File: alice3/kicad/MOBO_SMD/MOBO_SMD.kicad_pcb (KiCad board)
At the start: 2 copper layers, 90.2 x 48.3 mm, 67 parts, among them CON1 MicroSD, J1 VGA, P1 CONN_01X05, P2 USB_OTG, P3 UART1, SW1 RESET, SW2 SOFT RESET, U1 Z80CPU-SMD, U2 Propeller_P8X32A-Q44, U3 24LC256, U4 Propeller_Plug, U5 STM32F415RG, U6 AS6C2008_TSOP, U8 LD29080DT33R, X1 MINI_DIN_6, Y1 5 MHz, Y2 16MHz

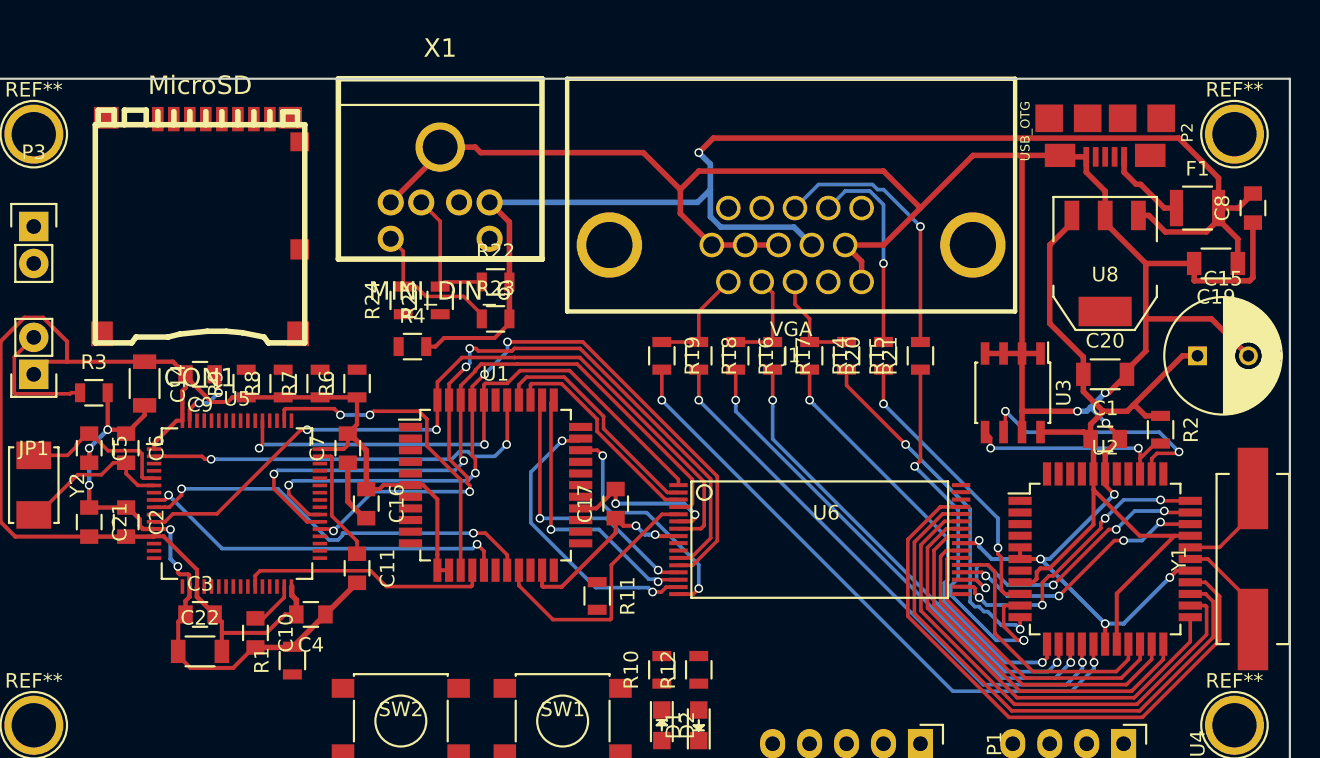
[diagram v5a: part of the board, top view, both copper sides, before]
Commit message: Switch to new MicroSD footprint and new Prop crystal.
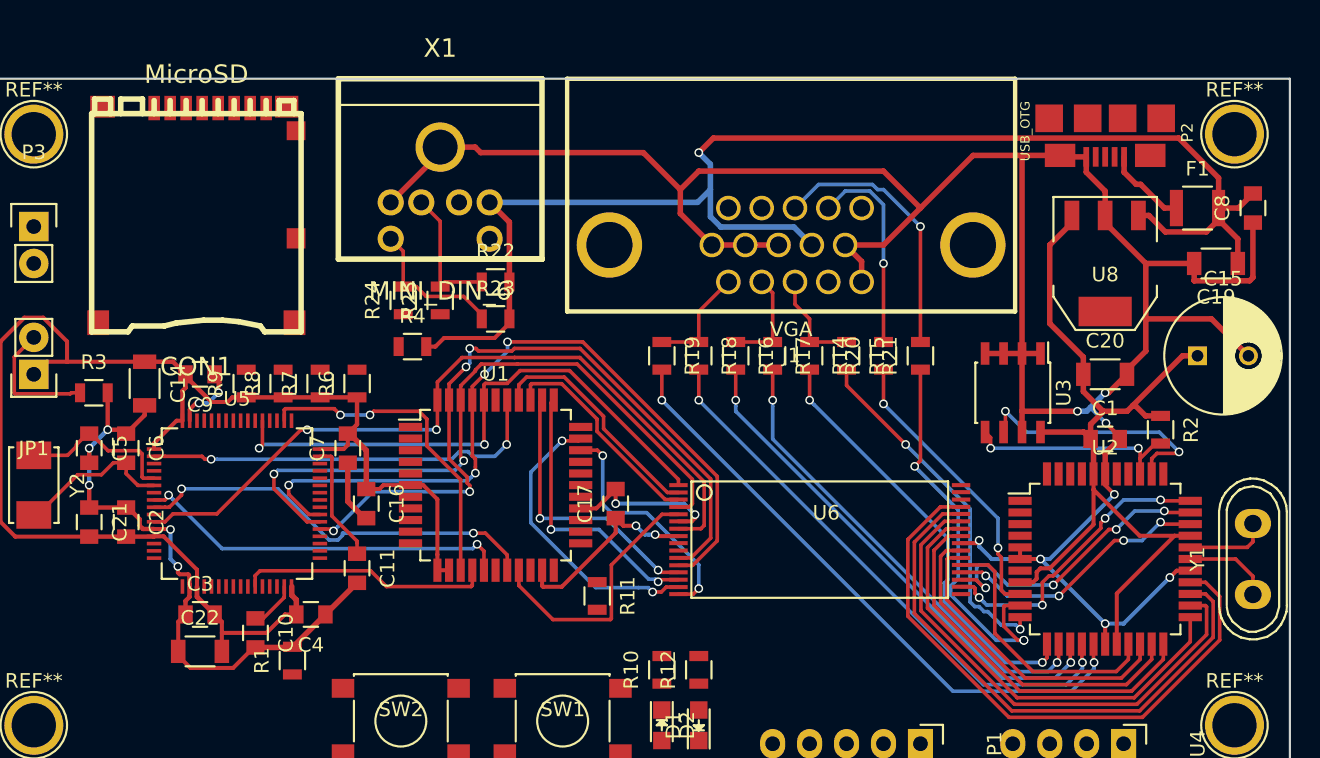
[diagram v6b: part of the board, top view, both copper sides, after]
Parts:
- Y1: footprint Crystals:Crystal_HC49-SD_SMD -> Crystals:Crystal_HC50-U_Vertical
- moved CON1 0.80 mm to (124.2, 83.1)
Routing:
- net Net-(U2-Pad28): track 7.34 -> 6.05 mm
- net Net-(U2-Pad29): track 7.01 -> 5.72 mm
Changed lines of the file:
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@@
   (general
     (links 246)
-    (no_connects 145)
-    (area 100.285476 67.307599 232.63921 175.29)
+    (no_connects 97)
+    (area 109.144999 73.584999 199.465001 121.995001)
     (thickness 1.6)
     (drawings 4)
@@
   )
   (module microsd:microsd_socket (layer F.Cu)
-    (at 124.46 83.82)
+    (at 124.206 83.058)
     (descr "MicroSD Card socket, Molex P/N 502774-0811")
     (fp_text reference CON1 (at 0 10.39876) (layer F.SilkS)
@@
       (net 100 "Net-(X1-Pad2)"))
   )
-  (module Crystals:Crystal_HC49-SD_SMD (layer F.Cu)
-    (at 196.85 106.68 90)
-    (descr "Crystal, Quarz, HC49-SD, SMD,")
-    (tags "Crystal, Quarz, HC49-SD, SMD,")
-    (attr smd)
-    (fp_text reference Y1 (at 0 -5.08 90) (layer F.SilkS)
-      (effects (font (size 1 1) (thickness 0.15)))
-    )
-    (fp_text value "5 MHz" (at 2.54 5.08 90) (layer F.Fab)
-      (effects (font (size 1 1) (thickness 0.15)))
-    )
-    (fp_circle (center 0 0) (end 0.8509 0) (layer F.Adhes) (width 0.381))
-    (fp_circle (center 0 0) (end 0.50038 0) (layer F.Adhes) (width 0.381))
-    (fp_circle (center 0 0) (end 0.14986 0.0508) (layer F.Adhes) (width 0.381))
-    (fp_line (start -5.84962 2.49936) (end 5.84962 2.49936) (layer F.SilkS) (width 0.15))
-    (fp_line (start 5.84962 -2.49936) (end -5.84962 -2.49936) (layer F.SilkS) (width 0.15))
-    (fp_line (start 5.84962 2.49936) (end 5.84962 1.651) (layer F.SilkS) (width 0.15))
-    (fp_line (start 5.84962 -2.49936) (end 5.84962 -1.651) (layer F.SilkS) (width 0.15))
-    (fp_line (start -5.84962 2.49936) (end -5.84962 1.651) (layer F.SilkS) (width 0.15))
-    (fp_line (start -5.84962 -2.49936) (end -5.84962 -1.651) (layer F.SilkS) (width 0.15))
-    (pad 1 smd rect (at -4.84886 0 90) (size 5.6007 2.10058) (layers F.Cu F.Paste F.Mask)
-      (net 93 "Net-(U2-Pad28)"))
-    (pad 2 smd rect (at 4.84886 0 90) (size 5.6007 2.10058) (layers F.Cu F.Paste F.Mask)
-      (net 94 "Net-(U2-Pad29)"))
-  )
   (module Crystals:ABM3 (layer F.Cu)
     (at 113.03 101.6 270)
@@
     (pad 1 thru_hole circle (at 0 0) (size 4.064 4.064) (drill 3.048) (layers *.Cu *.Mask F.SilkS))
   )
+  (module Crystals:Crystal_HC50-U_Vertical (layer F.Cu)
+    (at 196.85 106.68 90)
+    (descr "Crystal, Quarz, HC50/U, vertical, stehend,")
+    (tags "Crystal, Quarz, HC50/U, vertical, stehend,")
+    (fp_text reference Y1 (at 0 -3.81 90) (layer F.SilkS)
+      (effects (font (size 1 1) (thickness 0.15)))
+    )
+    (fp_text value "5 MHz" (at 0 3.81 90) (layer F.Fab)
+      (effects (font (size 1 1) (thickness 0.15)))
+    )
+    (fp_line (start 4.699 -1.00076) (end 4.89966 -0.59944) (layer F.SilkS) (width 0.15))
+    (fp_line (start 4.89966 -0.59944) (end 5.00126 0) (layer F.SilkS) (width 0.15))
+    (fp_line (start 5.00126 0) (end 4.89966 0.50038) (layer F.SilkS) (width 0.15))
+    (fp_line (start 4.89966 0.50038) (end 4.50088 1.19888) (layer F.SilkS) (width 0.15))
+    (fp_line (start 4.50088 1.19888) (end 3.8989 1.6002) (layer F.SilkS) (width 0.15))
+    (fp_line (start 3.8989 1.6002) (end 3.29946 1.80086) (layer F.SilkS) (width 0.15))
+    (fp_line (start 3.29946 1.80086) (end -3.29946 1.80086) (layer F.SilkS) (width 0.15))
+    (fp_line (start -3.29946 1.80086) (end -4.0005 1.6002) (layer F.SilkS) (width 0.15))
+    (fp_line (start -4.0005 1.6002) (end -4.39928 1.30048) (layer F.SilkS) (width 0.15))
+    (fp_line (start -4.39928 1.30048) (end -4.8006 0.8001) (layer F.SilkS) (width 0.15))
+    (fp_line (start -4.8006 0.8001) (end -5.00126 0.20066) (layer F.SilkS) (width 0.15))
+    (fp_line (start -5.00126 0.20066) (end -5.00126 -0.29972) (layer F.SilkS) (width 0.15))
+    (fp_line (start -5.00126 -0.29972) (end -4.8006 -0.8001) (layer F.SilkS) (width 0.15))
+    (fp_line (start -4.8006 -0.8001) (end -4.30022 -1.39954) (layer F.SilkS) (width 0.15))
+    (fp_line (start -4.30022 -1.39954) (end -3.79984 -1.69926) (layer F.SilkS) (width 0.15))
+    (fp_line (start -3.79984 -1.69926) (end -3.29946 -1.80086) (layer F.SilkS) (width 0.15))
+    (fp_line (start -3.2004 -1.80086) (end 3.40106 -1.80086) (layer F.SilkS) (width 0.15))
+    (fp_line (start 3.40106 -1.80086) (end 3.79984 -1.69926) (layer F.SilkS) (width 0.15))
+    (fp_line (start 3.79984 -1.69926) (end 4.30022 -1.39954) (layer F.SilkS) (width 0.15))
+    (fp_line (start 4.30022 -1.39954) (end 4.8006 -0.89916) (layer F.SilkS) (width 0.15))
+    (fp_line (start -3.19024 -2.32918) (end -3.64998 -2.28092) (layer F.SilkS) (width 0.15))
+    (fp_line (start -3.64998 -2.28092) (end -4.04876 -2.16916) (layer F.SilkS) (width 0.15))
+    (fp_line (start -4.04876 -2.16916) (end -4.48056 -1.95072) (layer F.SilkS) (width 0.15))
+    (fp_line (start -4.48056 -1.95072) (end -4.77012 -1.71958) (layer F.SilkS) (width 0.15))
+    (fp_line (start -4.77012 -1.71958) (end -5.10032 -1.36906) (layer F.SilkS) (width 0.15))
+    (fp_line (start -5.10032 -1.36906) (end -5.38988 -0.83058) (layer F.SilkS) (width 0.15))
+    (fp_line (start -5.38988 -0.83058) (end -5.51942 -0.23114) (layer F.SilkS) (width 0.15))
+    (fp_line (start -5.51942 -0.23114) (end -5.51942 0.2794) (layer F.SilkS) (width 0.15))
+    (fp_line (start -5.51942 0.2794) (end -5.34924 0.98044) (layer F.SilkS) (width 0.15))
+    (fp_line (start -5.34924 0.98044) (end -4.95046 1.56972) (layer F.SilkS) (width 0.15))
+    (fp_line (start -4.95046 1.56972) (end -4.49072 1.94056) (layer F.SilkS) (width 0.15))
+    (fp_line (start -4.49072 1.94056) (end -4.06908 2.14884) (layer F.SilkS) (width 0.15))
+    (fp_line (start -4.06908 2.14884) (end -3.6195 2.30886) (layer F.SilkS) (width 0.15))
+    (fp_line (start -3.6195 2.30886) (end -3.18008 2.33934) (layer F.SilkS) (width 0.15))
+    (fp_line (start 4.16052 2.1209) (end 4.53898 1.89992) (layer F.SilkS) (width 0.15))
+    (fp_line (start 4.53898 1.89992) (end 4.85902 1.62052) (layer F.SilkS) (width 0.15))
+    (fp_line (start 4.85902 1.62052) (end 5.11048 1.29032) (layer F.SilkS) (width 0.15))
+    (fp_line (start 5.11048 1.29032) (end 5.4102 0.73914) (layer F.SilkS) (width 0.15))
+    (fp_line (start 5.4102 0.73914) (end 5.51942 0.26924) (layer F.SilkS) (width 0.15))
+    (fp_line (start 5.51942 0.26924) (end 5.53974 -0.1905) (layer F.SilkS) (width 0.15))
+    (fp_line (start 5.53974 -0.1905) (end 5.45084 -0.65024) (layer F.SilkS) (width 0.15))
+    (fp_line (start 5.45084 -0.65024) (end 5.26034 -1.09982) (layer F.SilkS) (width 0.15))
+    (fp_line (start 5.26034 -1.09982) (end 4.89966 -1.56972) (layer F.SilkS) (width 0.15))
+    (fp_line (start 4.89966 -1.56972) (end 4.54914 -1.88976) (layer F.SilkS) (width 0.15))
+    (fp_line (start 4.54914 -1.88976) (end 4.16052 -2.1209) (layer F.SilkS) (width 0.15))
+    (fp_line (start 4.16052 -2.1209) (end 3.73126 -2.2606) (layer F.SilkS) (width 0.15))
+    (fp_line (start 3.73126 -2.2606) (end 3.2893 -2.32918) (layer F.SilkS) (width 0.15))
+    (fp_line (start -3.2004 2.32918) (end 3.2512 2.32918) (layer F.SilkS) (width 0.15))
+    (fp_line (start 3.2512 2.32918) (end 3.6703 2.29108) (layer F.SilkS) (width 0.15))
+    (fp_line (start 3.6703 2.29108) (end 4.16052 2.1209) (layer F.SilkS) (width 0.15))
+    (fp_line (start -3.2004 -2.32918) (end 3.2512 -2.32918) (layer F.SilkS) (width 0.15))
+    (pad 1 thru_hole oval (at -2.44094 0 90) (size 1.99898 2.49936) (drill 1.19888) (layers *.Cu *.Mask F.SilkS)
+      (net 93 "Net-(U2-Pad28)"))
+    (pad 2 thru_hole oval (at 2.44094 0 90) (size 1.99898 2.49936) (drill 1.19888) (layers *.Cu *.Mask F.SilkS)
+      (net 94 "Net-(U2-Pad29)"))
+  )
   (gr_line (start 109.22 121.92) (end 199.39 121.92) (angle 90) (layer Edge.Cuts) (width 0.15))
   (gr_line (start 109.22 73.66) (end 109.22 121.92) (angle 90) (layer Edge.Cuts) (width 0.15))
@@
   (segment (start 138.43 87.95) (end 138.43 85.52) (width 0.25) (layer F.Cu) (net 85) (status 10))
   (segment (start 138.43 85.52) (end 137.57 84.66) (width 0.25) (layer F.Cu) (net 85) (status 20))
-  (segment (start 192.54 106.68) (end 193.7512 106.68) (width 0.25) (layer F.Cu) (net 93) (status 10))
-  (segment (start 193.7512 106.68) (end 196.85 109.7788) (width 0.25) (layer F.Cu) (net 93) (status 20))
-  (segment (start 196.85 109.7788) (end 196.85 111.52886) (width 0.25) (layer F.Cu) (net 93) (status 30))
-  (segment (start 192.54 105.88) (end 194.5512 105.88) (width 0.25) (layer F.Cu) (net 94) (status 10))
-  (segment (start 194.5512 105.88) (end 196.85 103.5812) (width 0.25) (layer F.Cu) (net 94) (status 20))
-  (segment (start 196.85 103.5812) (end 196.85 101.83114) (width 0.25) (layer F.Cu) (net 94) (status 30))
+  (segment (start 192.54 106.68) (end 195.65855 106.68) (width 0.25) (layer F.Cu) (net 93))
+  (segment (start 195.65855 106.68) (end 196.85 107.87145) (width 0.25) (layer F.Cu) (net 93))
+  (segment (start 196.85 107.87145) (end 196.85 109.12094) (width 0.25) (layer F.Cu) (net 93))
+  (segment (start 192.54 105.88) (end 196.45855 105.88) (width 0.25) (layer F.Cu) (net 94))
+  (segment (start 196.85 105.48855) (end 196.85 104.23906) (width 0.25) (layer F.Cu) (net 94))
+  (segment (start 196.45855 105.88) (end 196.85 105.48855) (width 0.25) (layer F.Cu) (net 94))
   (segment (start 179.832 96.52) (end 179.832 97.823) (width 0.25) (layer F.Cu) (net 95))
   (segment (start 179.832 97.823) (end 179.705 97.95) (width 0.25) (layer F.Cu) (net 95))

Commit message: Change design rules to match OSHPark.
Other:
- net class Default: clearance 0.2 -> 0.1524; trace_width 0.25 -> 0.1524
- net class Power: clearance 0.2 -> 0.1524
- rule trace_clearance: 0.2 -> 0.1524
- rule trace_min: 0.2 -> 0.1524
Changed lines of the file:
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@@
   )
   (setup
-    (last_trace_width 0.25)
-    (trace_clearance 0.2)
+    (last_trace_width 0.1524)
+    (trace_clearance 0.1524)
     (zone_clearance 0.508)
     (zone_45_only no)
-    (trace_min 0.2)
+    (trace_min 0.1524)
     (segment_width 0.2)
     (edge_width 0.15)
@@
   (net 100 "Net-(X1-Pad2)")
   (net_class Default "This is the default net class."
-    (clearance 0.2)
-    (trace_width 0.25)
+    (clearance 0.1524)
+    (trace_width 0.1524)
     (via_dia 0.6)
     (via_drill 0.4)
@@
   )
   (net_class Power ""
-    (clearance 0.2)
+    (clearance 0.1524)
     (trace_width 0.2794)
     (via_dia 0.6)

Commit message: More routing.
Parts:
- moved C9 1.27 mm to (124.5, 92.7)
- moved R6 1.27 mm to (135.3, 93.3)
- moved R7 1.27 mm to (132.7, 93.3)
- moved R8 1.21 mm to (130.2, 93.4)
- moved R9 1.21 mm to (127.6, 93.4)
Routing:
- net GND: track 244.2 -> 376.1 mm, vias 17 -> 22
- net D0: track 18.4 -> 86.3 mm, vias 0 -> 4
- net A16: track 0.00 -> 57.4 mm, vias 0 -> 2
- net /MREQ: track 17.3 -> 60.5 mm, vias 0 -> 4
- net /BUSACK: track 0.00 -> 42.7 mm, vias 0 -> 4
- net VGA_R0: track 42.4 -> 0.00 mm, vias 2 -> 0
- net A2: track 20.6 -> 60.1 mm, vias 4 -> 6
- net VGA_R1: track 38.7 -> 0.00 mm, vias 2 -> 0
- net VGA_G1: track 35.2 -> 0.00 mm, vias 2 -> 0
- net D3: track 26.2 -> 61.2 mm, vias 0 -> 4
- net A4: track 16.5 -> 50.4 mm, vias 2 -> 4
- net D2: track 23.4 -> 56.3 mm, vias 0 -> 2
- net VGA_G0: track 32.5 -> 0.00 mm, vias 2 -> 0
- net /Z80_RESET: track 0.00 -> 31.7 mm, vias 0 -> 4
- net /WR: track 18.2 -> 48.3 mm, vias 0 -> 2
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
